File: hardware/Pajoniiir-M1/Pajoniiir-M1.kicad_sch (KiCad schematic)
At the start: 0 parts

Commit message: hardware: insert system shunt into 5V root power path
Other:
- sheet 01_POWER_INPUT ports: added 5V_PROTECTED; removed 5V_SYS
- sheet 14_TEST_MONITORING ports: added 3V3_SYS, 5V_PROTECTED, 5V_SYS, I2C_SCL, I2C_SDA, SYS_POWER_ALERT_N; removed none
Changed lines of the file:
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@@
       (effects (font (size 1.27 1.27)) (justify left))
     )
-    (pin "5V_SYS" input
+    (pin "5V_PROTECTED" input
       (at 65 25 0)
       (effects (font (size 1.27 1.27)) (justify right))
@@
   (sheet
     (at 75 145)
-    (size 45 18)
+    (size 45 34)
     (fields_autoplaced yes)
     (stroke (width 0.1524) (type solid))
@@
     )
     (property "Sheetfile" "14_TEST_MONITORING.kicad_sch"
-      (at 75 164.8246 0)
-      (effects (font (size 1.27 1.27)) (justify left top))
-    )
+      (at 75 180.8246 0)
+      (effects (font (size 1.27 1.27)) (justify left top))
+    )
+    (pin "5V_PROTECTED" output (at 75 149 180) (effects (font (size 1.27 1.27)) (justify left)))
+    (pin "5V_SYS" input (at 120 149 0) (effects (font (size 1.27 1.27)) (justify right)))
+    (pin "3V3_SYS" output (at 75 155 180) (effects (font (size 1.27 1.27)) (justify left)))
+    (pin "I2C_SDA" bidirectional (at 120 155 0) (effects (font (size 1.27 1.27)) (justify right)))
+    (pin "I2C_SCL" output (at 120 159 0) (effects (font (size 1.27 1.27)) (justify right)))
+    (pin "SYS_POWER_ALERT_N" input (at 120 165 0) (effects (font (size 1.27 1.27)) (justify right)))
     (instances
       (project "Pajoniiir-M1"
@@
     )
   )
-  (wire (pts (xy 65 25) (xy 75 25)) (stroke (width 0) (type default)))
   (wire (pts (xy 120 23) (xy 125 23) (xy 125 25) (xy 130 25)) (stroke (width 0) (type default)))
   (wire (pts (xy 175 69) (xy 185 69)) (stroke (width 0) (type default)))
@@
   (label "C6_BOOT_GPIO8" (at 65 75 0) (effects (font (size 1.27 1.27))))
   (label "C6_BOOT_GPIO9" (at 65 77 0) (effects (font (size 1.27 1.27))))
+  (label "5V_PROTECTED" (at 75 149 180) (effects (font (size 1.27 1.27))))
+  (label "5V_SYS" (at 120 149 0) (effects (font (size 1.27 1.27))))
+  (label "3V3_SYS" (at 75 155 180) (effects (font (size 1.27 1.27))))
+  (label "I2C_SDA" (at 120 155 0) (effects (font (size 1.27 1.27))))
+  (label "I2C_SCL" (at 120 159 0) (effects (font (size 1.27 1.27))))
+  (label "SYS_POWER_ALERT_N" (at 120 165 0) (effects (font (size 1.27 1.27))))
+  (label "5V_PROTECTED" (at 65 25 0) (effects (font (size 1.27 1.27))))
+  (label "5V_SYS" (at 75 25 180) (effects (font (size 1.27 1.27))))
+  (label "3V3_SYS" (at 120 23 0) (effects (font (size 1.27 1.27))))
+  (label "I2C_SDA" (at 175 29 0) (effects (font (size 1.27 1.27))))
+  (label "I2C_SCL" (at 175 31 0) (effects (font (size 1.27 1.27))))
+  (label "SYS_POWER_ALERT_N" (at 175 59 0) (effects (font (size 1.27 1.27))))
   (sheet_instances (path "/" (page "1")))
   (embedded_fonts no)

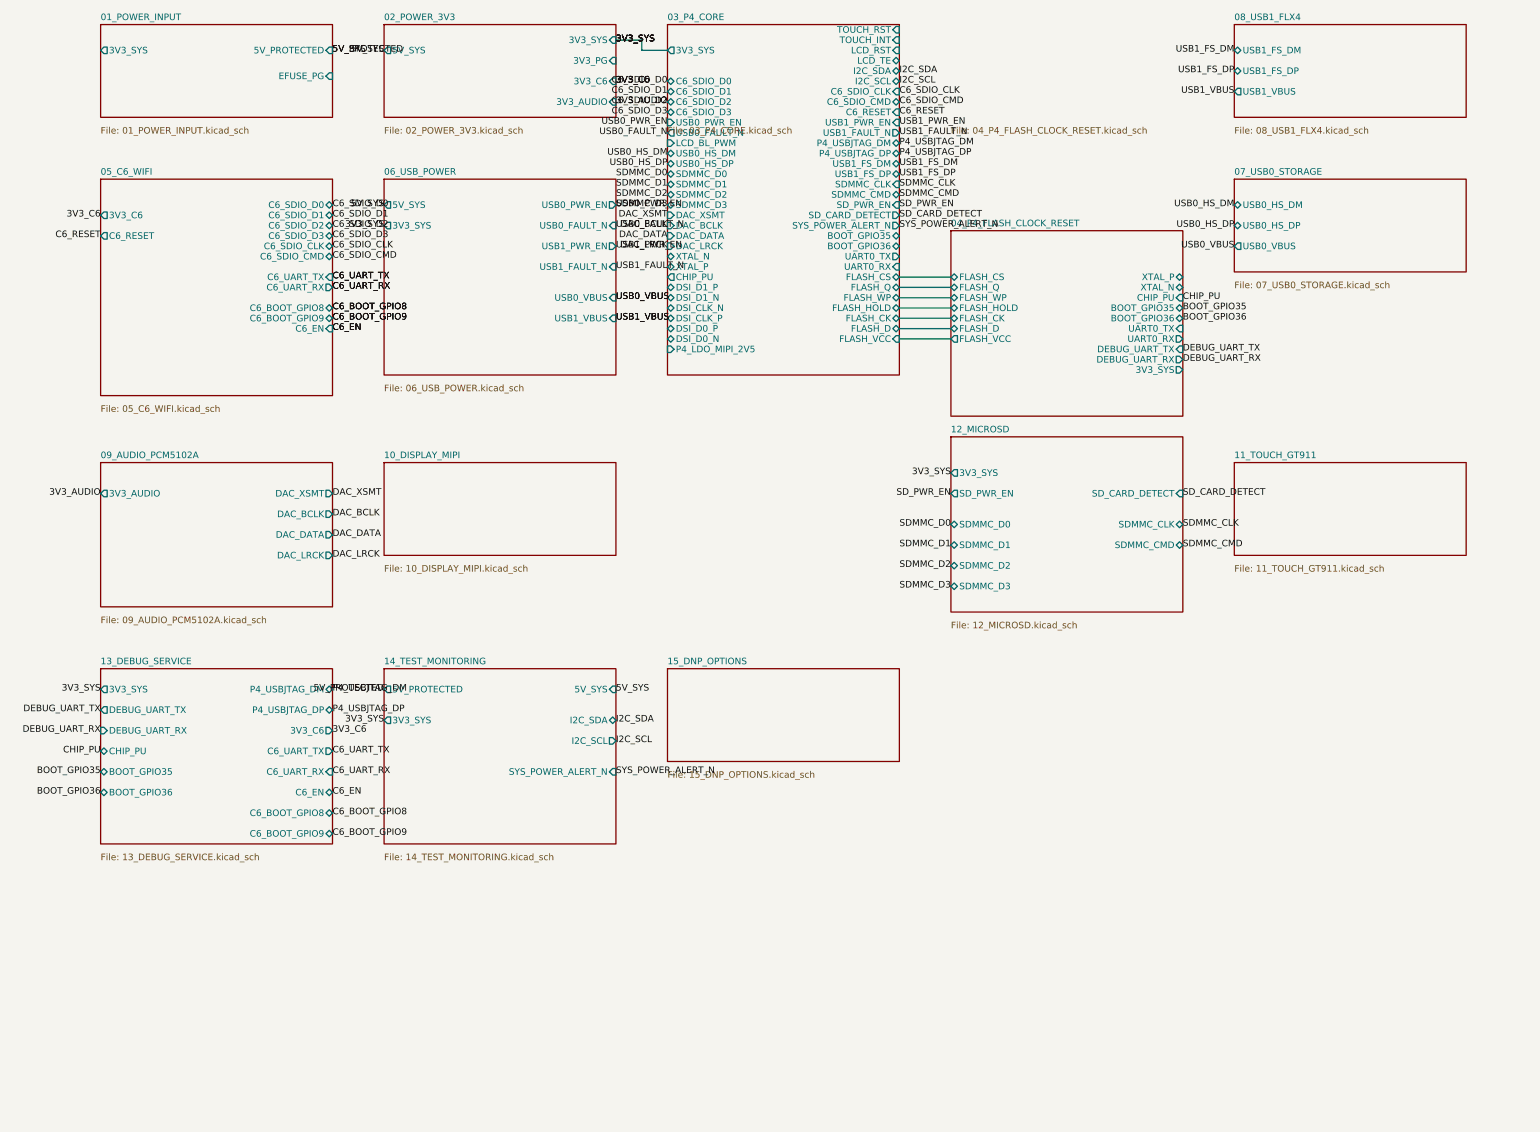
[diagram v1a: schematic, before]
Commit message: hardware: wire MIPI display hierarchy
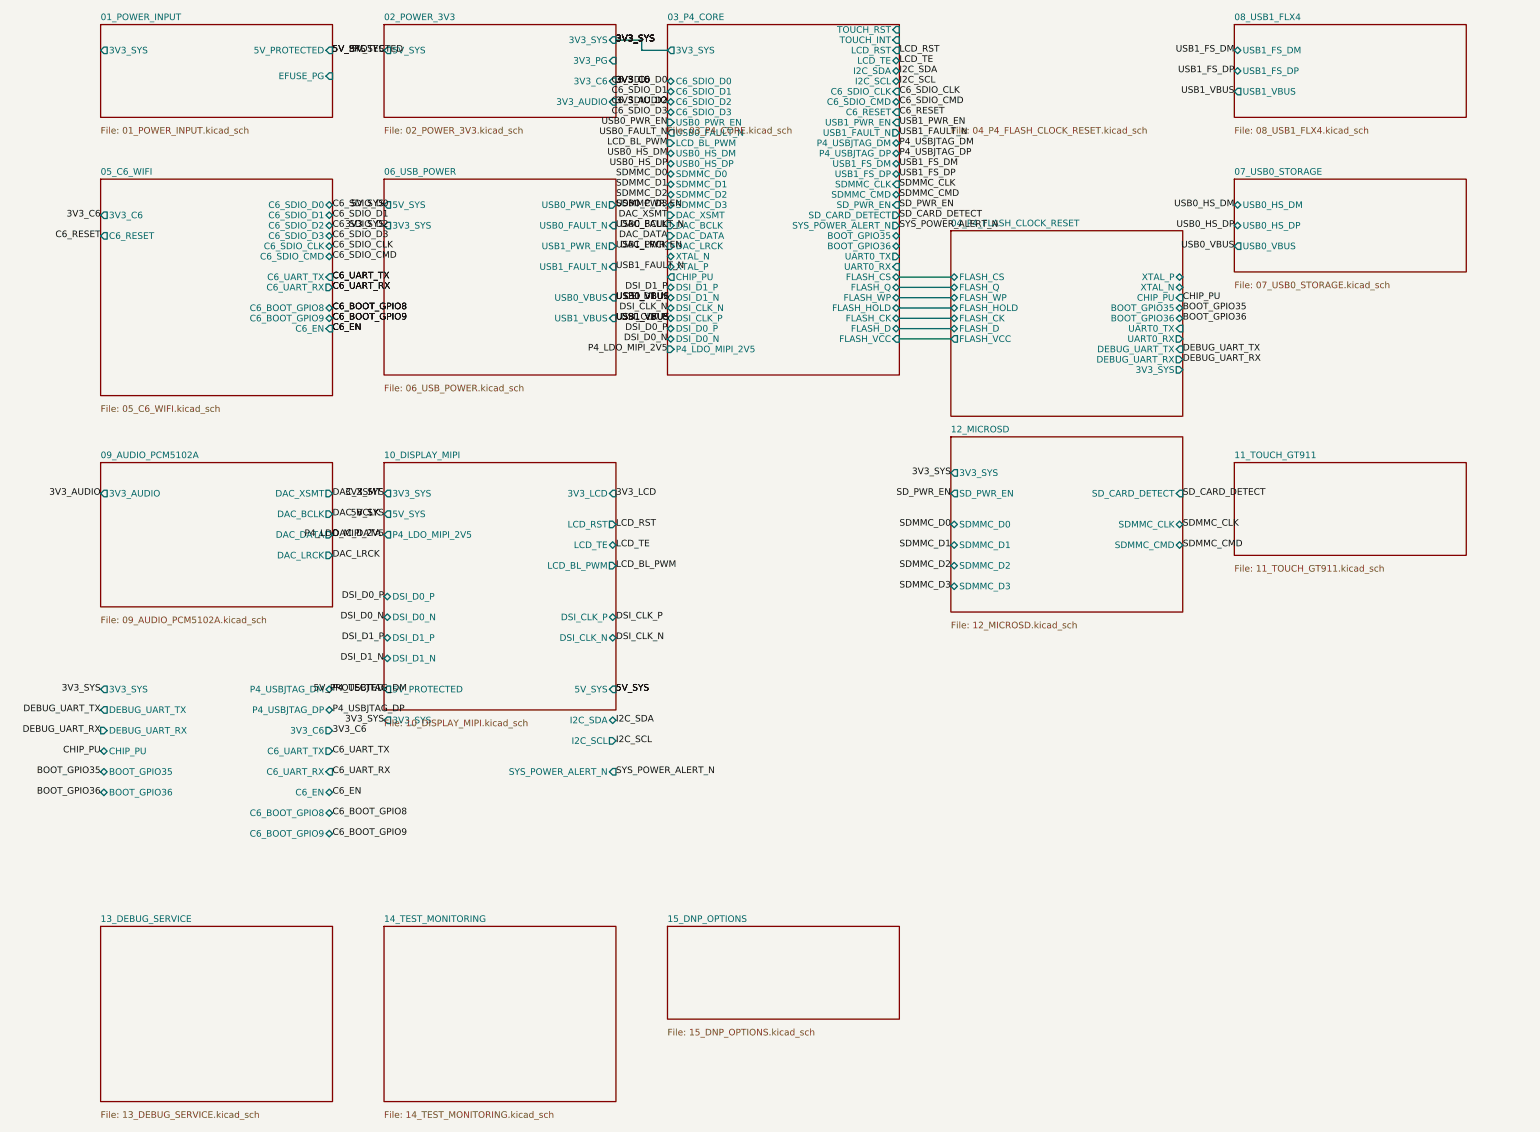
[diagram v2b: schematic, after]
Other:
- sheet 10_DISPLAY_MIPI ports: added 3V3_LCD, 3V3_SYS, 5V_SYS, DSI_CLK_N, DSI_CLK_P, DSI_D0_N, DSI_D0_P, DSI_D1_N, DSI_D1_P, LCD_BL_PWM, LCD_RST, LCD_TE, P4_LDO_MIPI_2V5; removed none
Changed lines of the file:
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@@
   (sheet
     (at 75 105)
-    (size 45 18)
+    (size 45 48)
     (fields_autoplaced yes)
     (stroke (width 0.1524) (type solid))
@@
     )
     (property "Sheetfile" "10_DISPLAY_MIPI.kicad_sch"
-      (at 75 124.8246 0)
-      (effects (font (size 1.27 1.27)) (justify left top))
-    )
+      (at 75 154.8246 0)
+      (effects (font (size 1.27 1.27)) (justify left top))
+    )
+    (pin "3V3_SYS" output (at 75 111 180) (effects (font (size 1.27 1.27)) (justify left)))
+    (pin "5V_SYS" output (at 75 115 180) (effects (font (size 1.27 1.27)) (justify left)))
+    (pin "P4_LDO_MIPI_2V5" output (at 75 119 180) (effects (font (size 1.27 1.27)) (justify left)))
+    (pin "3V3_LCD" input (at 120 111 0) (effects (font (size 1.27 1.27)) (justify right)))
+    (pin "LCD_RST" output (at 120 117 0) (effects (font (size 1.27 1.27)) (justify right)))
+    (pin "LCD_TE" bidirectional (at 120 121 0) (effects (font (size 1.27 1.27)) (justify right)))
+    (pin "LCD_BL_PWM" output (at 120 125 0) (effects (font (size 1.27 1.27)) (justify right)))
+    (pin "DSI_D0_P" bidirectional (at 75 131 180) (effects (font (size 1.27 1.27)) (justify left)))
+    (pin "DSI_D0_N" bidirectional (at 75 135 180) (effects (font (size 1.27 1.27)) (justify left)))
+    (pin "DSI_D1_P" bidirectional (at 75 139 180) (effects (font (size 1.27 1.27)) (justify left)))
+    (pin "DSI_D1_N" bidirectional (at 75 143 180) (effects (font (size 1.27 1.27)) (justify left)))
+    (pin "DSI_CLK_P" bidirectional (at 120 135 0) (effects (font (size 1.27 1.27)) (justify right)))
+    (pin "DSI_CLK_N" bidirectional (at 120 139 0) (effects (font (size 1.27 1.27)) (justify right)))
     (instances
       (project "Pajoniiir-M1"
@@
   )
   (sheet
-    (at 20 145)
+    (at 20 195)
     (size 45 34)
     (fields_autoplaced yes)
@@
     (fill (color 0 0 0 0.0000))
     (property "Sheetname" "13_DEBUG_SERVICE"
-      (at 20 144.2888 0)
+      (at 20 194.2888 0)
       (effects (font (size 1.27 1.27)) (justify left bottom))
     )
     (property "Sheetfile" "13_DEBUG_SERVICE.kicad_sch"
-      (at 20 180.8246 0)
+      (at 20 230.8246 0)
       (effects (font (size 1.27 1.27)) (justify left top))
     )
@@
   )
   (sheet
-    (at 75 145)
+    (at 75 195)
     (size 45 34)
     (fields_autoplaced yes)
@@
     (fill (color 0 0 0 0.0000))
     (property "Sheetname" "14_TEST_MONITORING"
-      (at 75 144.2888 0)
+      (at 75 194.2888 0)
       (effects (font (size 1.27 1.27)) (justify left bottom))
     )
     (property "Sheetfile" "14_TEST_MONITORING.kicad_sch"
-      (at 75 180.8246 0)
+      (at 75 230.8246 0)
       (effects (font (size 1.27 1.27)) (justify left top))
     )
@@
   )
   (sheet
-    (at 130 145)
+    (at 130 195)
     (size 45 18)
     (fields_autoplaced yes)
@@
     (fill (color 0 0 0 0.0000))
     (property "Sheetname" "15_DNP_OPTIONS"
-      (at 130 144.2888 0)
+      (at 130 194.2888 0)
       (effects (font (size 1.27 1.27)) (justify left bottom))
     )
     (property "Sheetfile" "15_DNP_OPTIONS.kicad_sch"
-      (at 130 164.8246 0)
+      (at 130 214.8246 0)
       (effects (font (size 1.27 1.27)) (justify left top))
     )
@@
   (label "I2C_SCL" (at 175 31 0) (effects (font (size 1.27 1.27))))
   (label "SYS_POWER_ALERT_N" (at 175 59 0) (effects (font (size 1.27 1.27))))
+  (label "3V3_SYS" (at 75 111 180) (effects (font (size 1.27 1.27))))
+  (label "5V_SYS" (at 75 115 180) (effects (font (size 1.27 1.27))))
+  (label "P4_LDO_MIPI_2V5" (at 75 119 180) (effects (font (size 1.27 1.27))))
+  (label "3V3_LCD" (at 120 111 0) (effects (font (size 1.27 1.27))))
+  (label "LCD_RST" (at 120 117 0) (effects (font (size 1.27 1.27))))
+  (label "LCD_TE" (at 120 121 0) (effects (font (size 1.27 1.27))))
+  (label "LCD_BL_PWM" (at 120 125 0) (effects (font (size 1.27 1.27))))
+  (label "DSI_D0_P" (at 75 131 180) (effects (font (size 1.27 1.27))))
+  (label "DSI_D0_N" (at 75 135 180) (effects (font (size 1.27 1.27))))
+  (label "DSI_D1_P" (at 75 139 180) (effects (font (size 1.27 1.27))))
+  (label "DSI_D1_N" (at 75 143 180) (effects (font (size 1.27 1.27))))
+  (label "DSI_CLK_P" (at 120 135 0) (effects (font (size 1.27 1.27))))
+  (label "DSI_CLK_N" (at 120 139 0) (effects (font (size 1.27 1.27))))
+  (label "3V3_SYS" (at 120 23 0) (effects (font (size 1.27 1.27))))
+  (label "5V_SYS" (at 120 149 0) (effects (font (size 1.27 1.27))))
+  (label "P4_LDO_MIPI_2V5" (at 130 83 180) (effects (font (size 1.27 1.27))))
+  (label "LCD_RST" (at 175 25 0) (effects (font (size 1.27 1.27))))
+  (label "LCD_TE" (at 175 27 0) (effects (font (size 1.27 1.27))))
+  (label "LCD_BL_PWM" (at 130 43 180) (effects (font (size 1.27 1.27))))
+  (label "DSI_D1_P" (at 130 71 180) (effects (font (size 1.27 1.27))))
+  (label "DSI_D1_N" (at 130 73 180) (effects (font (size 1.27 1.27))))
+  (label "DSI_CLK_N" (at 130 75 180) (effects (font (size 1.27 1.27))))
+  (label "DSI_CLK_P" (at 130 77 180) (effects (font (size 1.27 1.27))))
+  (label "DSI_D0_P" (at 130 79 180) (effects (font (size 1.27 1.27))))
+  (label "DSI_D0_N" (at 130 81 180) (effects (font (size 1.27 1.27))))
   (sheet_instances (path "/" (page "1")))
   (embedded_fonts no)
